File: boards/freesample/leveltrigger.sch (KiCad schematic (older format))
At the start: 23 parts, among them U10 PI6C59S6005, U9 HMC675LP3E

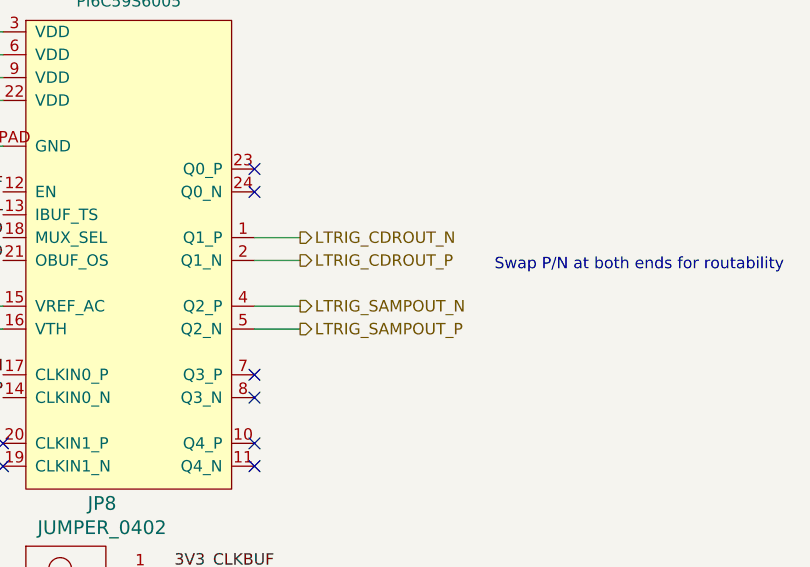
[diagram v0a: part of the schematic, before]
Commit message: Finished initial layout of level trigger and ADC subsystems
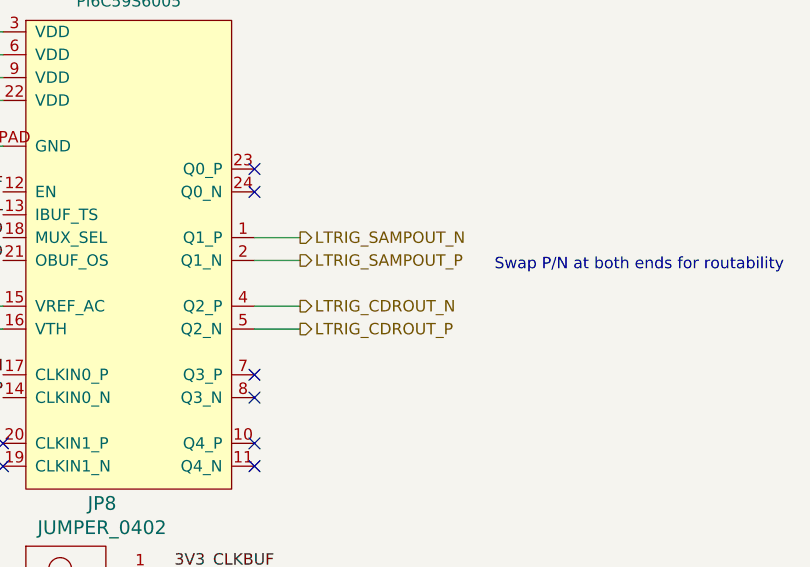
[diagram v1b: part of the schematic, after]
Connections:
- net LTRIG_CDROUT_N: now also U10.4 (Q2_P); no longer U10.1 (Q1_P)
- net LTRIG_CDROUT_P: now also U10.5 (Q2_N); no longer U10.2 (Q1_N)
- net LTRIG_SAMPOUT_N: now also U10.1 (Q1_P); no longer U10.4 (Q2_P)
- net LTRIG_SAMPOUT_P: now also U10.2 (Q1_N); no longer U10.5 (Q2_N)
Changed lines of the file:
@@
 Text HLabel 3750 3100 0    50   Input ~ 0
 LTRIG_VT
-Text HLabel 8850 2750 2    50   Output ~ 0
+Text HLabel 8850 2450 2    50   Output ~ 0
 LTRIG_SAMPOUT_P
-Text HLabel 8850 2650 2    50   Output ~ 0
+Text HLabel 8850 2350 2    50   Output ~ 0
 LTRIG_SAMPOUT_N
 $Comp
@@
 Wire Wire Line
 	8850 2350 8650 2350
-Text HLabel 8850 2350 2    50   Output ~ 0
+Text HLabel 8850 2650 2    50   Output ~ 0
 LTRIG_CDROUT_N
-Text HLabel 8850 2450 2    50   Output ~ 0
+Text HLabel 8850 2750 2    50   Output ~ 0
 LTRIG_CDROUT_P
 NoConn ~ 8650 2150
